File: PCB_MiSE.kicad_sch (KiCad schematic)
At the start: 20 parts, among them IC1 MSP430FR2355TPT, J2 Conn_01x03, SW1 SW_Push, SW2 SW_Push, SW3 SW_Push, U1 LM324, U2 LM324, Y1 Crystal

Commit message: MiSE 24/02
Pendings:
- Check final al sch (comparar con otros grupos).
- Acabar de asignar huellas.
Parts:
- removed R5: R, symbol Device:R
- removed U1, U2: LM324, symbol Amplifier_Operational:LM324
- removed Y1: Crystal, symbol Device:Crystal
- added C5: C, Capacitor_SMD:C_0805_2012Metric_Pad1.18x1.45mm_HandSolder, symbol Device:C
- added J1: WIFI, symbol Connector_Generic:Conn_02x04_Odd_Even
- added J3: Sensor Ultrasonido, symbol Connector_Generic:Conn_01x05
- added J5: Conn_02x07_Counter_Clockwise, symbol Connector_Generic:Conn_02x07_Counter_Clockwise
- added J6: Display, symbol Connector_Generic:Conn_02x04_Odd_Even
- added R10, R11, R8, R9: R, Resistor_SMD:R_0805_2012Metric_Pad1.20x1.40mm_HandSolder, symbol Device:R
- added RV1, RV2: R_Potentiometer_Trim, symbol Device:R_Potentiometer_Trim
- added SW4: SW_Push, Button_Switch_THT:SW_PUSH_6mm, symbol Switch:SW_Push
- added U1: LMV324, Package_SO:SOIC-14_3.9x8.7mm_P1.27mm, symbol Amplifier_Operational:LMV324
- added Y1: Crystal_GND3, Crystal:Crystal_DS26_D2.0mm_L6.0mm_Horizontal_1EP_style1, symbol Device:Crystal_GND3
- C1, C2, C3, C4: footprint (none) -> Capacitor_SMD:C_0805_2012Metric_Pad1.18x1.45mm_HandSolder
- IC1: footprint QFP50P900X900X160-48N -> (none)
- R1, R2, R3, R4, R6, R7: footprint (none) -> Resistor_SMD:R_0805_2012Metric_Pad1.20x1.40mm_HandSolder
- S1: footprint THB001P -> (none)
- SW1, SW2, SW3: footprint (none) -> Button_Switch_THT:SW_PUSH_6mm
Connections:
- net GND: now also C5.2, J1.7 (Pin_7), J3.5 (Pin_5), J5.7 (Pin_7), J5.8 (Pin_8), J6.2 (Pin_2), RV1.2, RV2.2, SW4.1, U1.11 (V-), Y1.3
- net VCC: now also C5.1, J1.2 (Pin_2), J3.1 (Pin_1), J5.1 (Pin_1), J5.14 (Pin_14), J6.1 (Pin_1), R10.1, R11.1, R8.1, R9.1, U1.4 (V+)
- net at S1.12 (2'): now also U1.12 (+), U1.9 (-)
- net at S1.2: now also U1.2 (-), U1.5 (+)
- net at IC1.47 (P3.0/MCLK), S1.C1 (NO_1): now also J5.5 (Pin_5)
- net at C4.1: now also Y1.2
- net at C3.1, IC1.8 (P2.7/TB0CLK/XIN): now also Y1.1
- net at IC1.10 (P2.5/COMP1.0): now also U1.1
- net at R1.2, R2.1: now also U1.10 (+), U1.3 (+)
- net at IC1.13 (P4.6/UCB1SIMO/UCB1SDA): now also U1.8
- net at R2.2, R3.1: now also U1.13 (-), U1.6 (-)
- net at IC1.14 (P4.5/UCB1CLK): now also U1.14
- net at IC1.11 (P2.4/COMP1.1): now also U1.7
- net at IC1.1 (P1.2/UCB0SIMO/UCB0SDA/TB0TRG/OA0-/A2/VEREF-): now also J5.6 (Pin_6), J6.3 (Pin_3)
- net at IC1.2 (P1.1/UCB0CLK/ACLK/OA0O/COMP0.1/A1): now also R8.2, RV2.1
- net at IC1.20 (P6.2/TB3.3): now also J5.13 (Pin_13)
- net at IC1.21 (P6.1/TB3.2): now also J5.12 (Pin_12)
- net at IC1.22 (P6.0/TB3.1): now also J3.2 (Pin_2)
- net at IC1.23 (P4.3/UCA1TXD/UCA1SIMO/~{UCA1TXD}): now also J3.3 (Pin_3)
- net at IC1.31 (P1.7/UCA0TXD/UCA0SIMO/TB0.2/TDO/OA1+/A7/VREF+): now also J1.8 (Pin_8)
- net at IC1.32 (P1.6/UCA0RXD/UCA0SOMI/TB0.1/TDI/TCLK/OA1-/A6): now also J1.1 (Pin_1)
- net at IC1.34 (P1.4/UCA0STE/TCK/A4): now also R11.2, RV1.1
- net at IC1.48 (P1.3/UCB0SOMI/UCB0SCL/OA0+/A3): now also J6.4 (Pin_4)
- new net: J6.5 (Pin_5), R9.2, SW4.2
- new net: J1.6 (Pin_6), R10.2
- no-connect marks 6 -> 46
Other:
- moved on the sheet: C1, C2, C3, C4, IC1, J2, R1, R2, R3, R4, R6, R7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

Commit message: MiSE 24/02
Pendings:
- revisar sch
- actualizar todas las huellas
- poner todos los footprint dentro del proyecto
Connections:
- net GND: now also SW1.1
- net at IC1.5 (~{RST}/NMI/SBWTDIO), J2.2 (Pin_2): now also C1.1, R4.2, SW1.2; no longer SW1.1
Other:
- note removed: "footprint reset: SW_PUSH_6mm"
- moved on the sheet: SW1

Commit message: Add files via upload
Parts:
- removed C5: C, Capacitor_SMD:C_0805_2012Metric_Pad1.18x1.45mm_HandSolder, symbol Device:C
- removed J3: Sensor Ultrasonido, symbol Connector_Generic:Conn_01x05
- removed J5: Conn_02x07_Counter_Clockwise, symbol Connector_Generic:Conn_02x07_Counter_Clockwise
- removed R11, R8: R, Resistor_SMD:R_0805_2012Metric_Pad1.20x1.40mm_HandSolder, symbol Device:R
- added D1: LED, LED_SMD:LED_0805_2012Metric_Pad1.15x1.40mm_HandSolder, symbol Device:LED
- added J4: Clk read conn, Connector_PinHeader_2.54mm:PinHeader_1x02_P2.54mm_Vertical, symbol Connector_Generic:Conn_01x02
- added J7: I2C read, Connector_PinHeader_2.54mm:PinHeader_1x02_P2.54mm_Vertical_SMD_Pin1Left, symbol Connector_Generic:Conn_01x02
- added J8: Conn_02x07_Odd_Even, MSP430:conn_DFrobot, symbol Connector_Generic:Conn_02x07_Odd_Even
- added R12, R13, R14, R5: R, Resistor_SMD:R_0805_2012Metric_Pad1.20x1.40mm_HandSolder, symbol Device:R
- added R15, R8: LDR03, OptoDevice:R_LDR_10x8.5mm_P7.6mm_Vertical, symbol Sensor_Optical:LDR03
- IC1: footprint (none) -> MSP430:QFP50P900X900X160-48N
- J2: footprint (none) -> Connector_PinHeader_2.54mm:PinHeader_1x03_P2.54mm_Vertical
- J6: footprint (none) -> MSP430:LCD_2x16_I2C(Midas)
- RV1, RV2: footprint (none) -> MSP430:Trimmer_MiSE
- S1: footprint (none) -> MSP430:THB001P
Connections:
- net GND: now also S1.C1 (NO_1), J8.13 (Pin_13), J8.14 (Pin_14), R14.2
- net VCC: now also J8.1 (Pin_1), J8.2 (Pin_2), R12.1, R13.1, R15.1, R5.1, R8.1
- net at S1.2, U1.2 (-), U1.5 (+): now also U1.3 (+)
- net at IC1.46 (P3.1/OA2O), S1.B1 (COM_2): now also R5.2
- net at IC1.47 (P3.0/MCLK): no longer S1.C1 (NO_1)
- net TDO/TDI: now reaches C1.1, IC1.5 (~{RST}/NMI/SBWTDIO), R4.2, SW1.2
- net TDO/TDI: now also J2.3 (Pin_3); no longer J2.2 (Pin_2)
- net SDA: now reaches IC1.1 (P1.2/UCB0SIMO/UCB0SDA/TB0TRG/OA0-/A2/VEREF-), J6.3 (Pin_3)
- net SDA: now also J7.1 (Pin_1), J8.11 (Pin_11), R12.2
- net SCL: now reaches IC1.48 (P1.3/UCB0SOMI/UCB0SCL/OA0+/A3), J6.4 (Pin_4)
- net SCL: now also J7.2 (Pin_2), J8.9 (Pin_9), R13.2
- net at C4.1, Y1.2: now also IC1.9 (P2.6/MCLK/XOUT)
- net GPIOl: now reaches U1.7
- net GPIOl: now also IC1.10 (P2.5/COMP1.0); no longer IC1.11 (P2.4/COMP1.1)
- net TCK: now reaches IC1.4 (TEST/SBWTCK)
- net TCK: now also J2.2 (Pin_2); no longer J2.3 (Pin_3)
- net at IC1.34 (P1.4/UCA0STE/TCK/A4), RV1.1: now also R8.2
- net at RV2.1: now also IC1.45 (P3.2/OA2-), R15.2; no longer IC1.2 (P1.1/UCB0CLK/ACLK/OA0O/COMP0.1/A1)
- net at R1.2, R2.1, U1.10 (+): no longer U1.3 (+)
- net P1: now reaches IC1.21 (P6.1/TB3.2)
- net P1: now also J8.6 (Pin_6)
- net P0: now reaches IC1.20 (P6.2/TB3.3)
- net P0: now also J8.4 (Pin_4)
- net CH_EN: now reaches J1.6 (Pin_6), R10.2
- net GPIOr': now reaches IC1.13 (P4.6/UCB1SIMO/UCB1SDA), U1.8
- net GPIOr: now reaches U1.1
- net GPIOr: now also IC1.11 (P2.4/COMP1.1); no longer IC1.10 (P2.5/COMP1.0)
- net U0RXD: now reaches J1.1 (Pin_1)
- net U0RXD: now also IC1.31 (P1.7/UCA0TXD/UCA0SIMO/TB0.2/TDO/OA1+/A7/VREF+); no longer IC1.32 (P1.6/UCA0RXD/UCA0SOMI/TB0.1/TDI/TCLK/OA1-/A6)
- net U0TXD: now reaches J1.8 (Pin_8)
- net U0TXD: now also IC1.32 (P1.6/UCA0RXD/UCA0SOMI/TB0.1/TDI/TCLK/OA1-/A6); no longer IC1.31 (P1.7/UCA0TXD/UCA0SIMO/TB0.2/TDO/OA1+/A7/VREF+)
- net GPIOl': now reaches IC1.14 (P4.5/UCB1CLK), U1.14
- net P8: now reaches IC1.15 (P4.4/UCB1STE)
- net P8: now also J8.10 (Pin_10)
- net P2: now reaches IC1.17 (P6.5/TB3.6)
- net P2: now also J8.8 (Pin_8)
- net at IC1.19 (P6.3/TB3.4): now also D1.2 (A)
- net at IC1.25 (P4.1/UCA1CLK): now also J8.12 (Pin_12)
- net at IC1.3 (P1.0/UCB0STE/SMCLK/COMP0.0/A0/VEREF+): now also J4.1 (Pin_1)
- new net: IC1.2 (P1.1/UCB0CLK/ACLK/OA0O/COMP0.1/A1), J4.2 (Pin_2)
- new net: D1.1 (K), R14.1
- no-connect marks 46 -> 38
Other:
- note added: "Buttons"
- note added: "Conn-Robot"
- note added: "Crystal"
- note added: "Display"
- note added: "Joystick"
- note added: "LDR1"
- note added: "LDR2"
- note added: "RST"
- note added: "SBW"
- note added: "Test-LED"
- note added: "Wi-FI"
- moved on the sheet: C1, C2, C3, C4, IC1, J1, J2, J6, R1, R10, R2, R3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

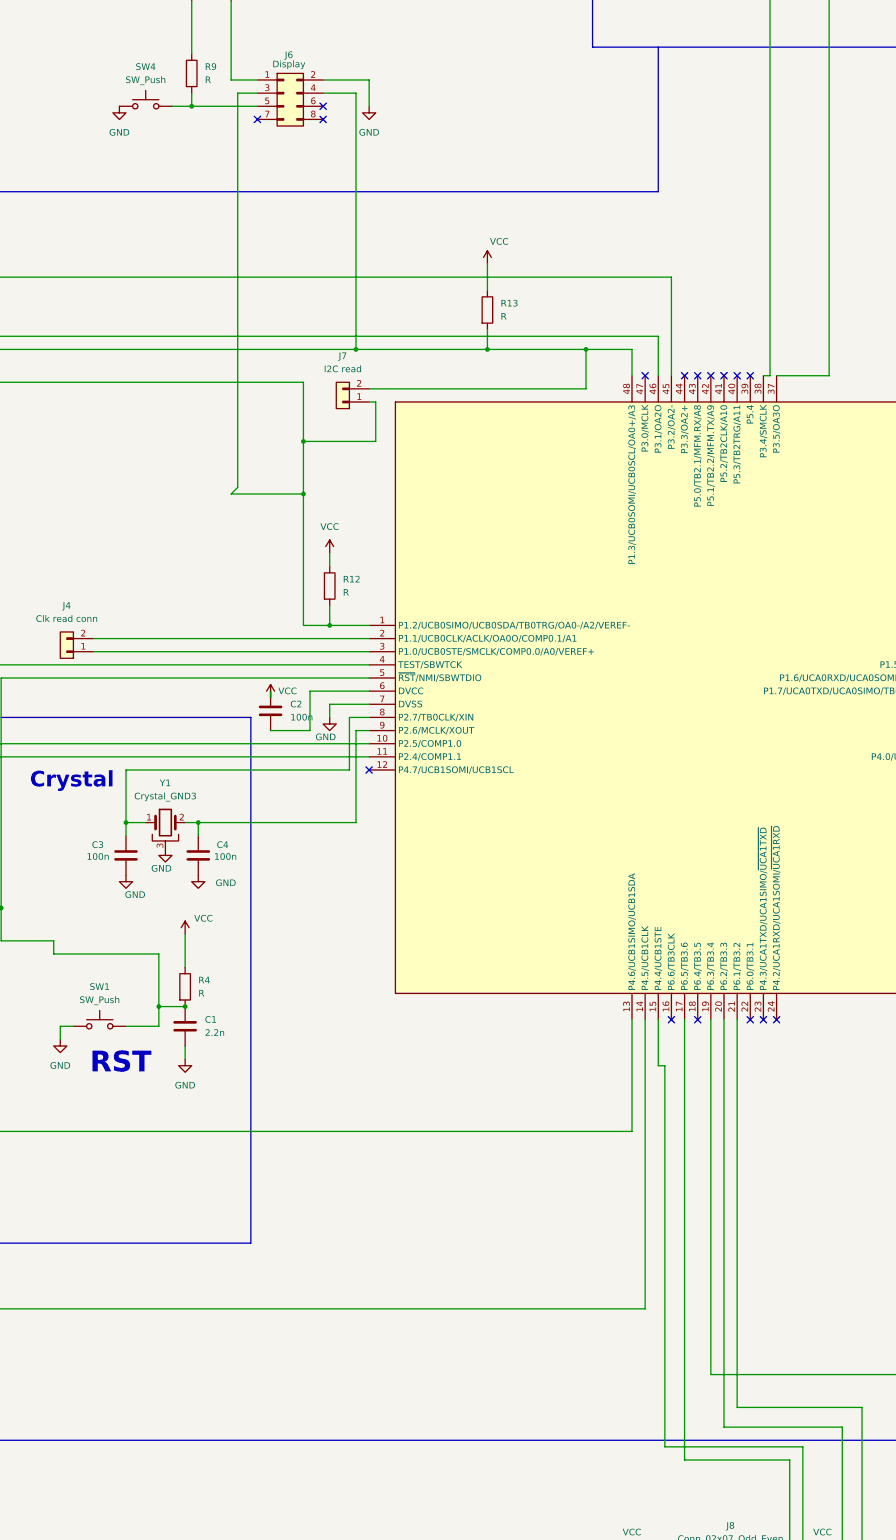
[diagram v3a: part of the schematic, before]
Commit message: Corrijo errores de diseño, DRC bien
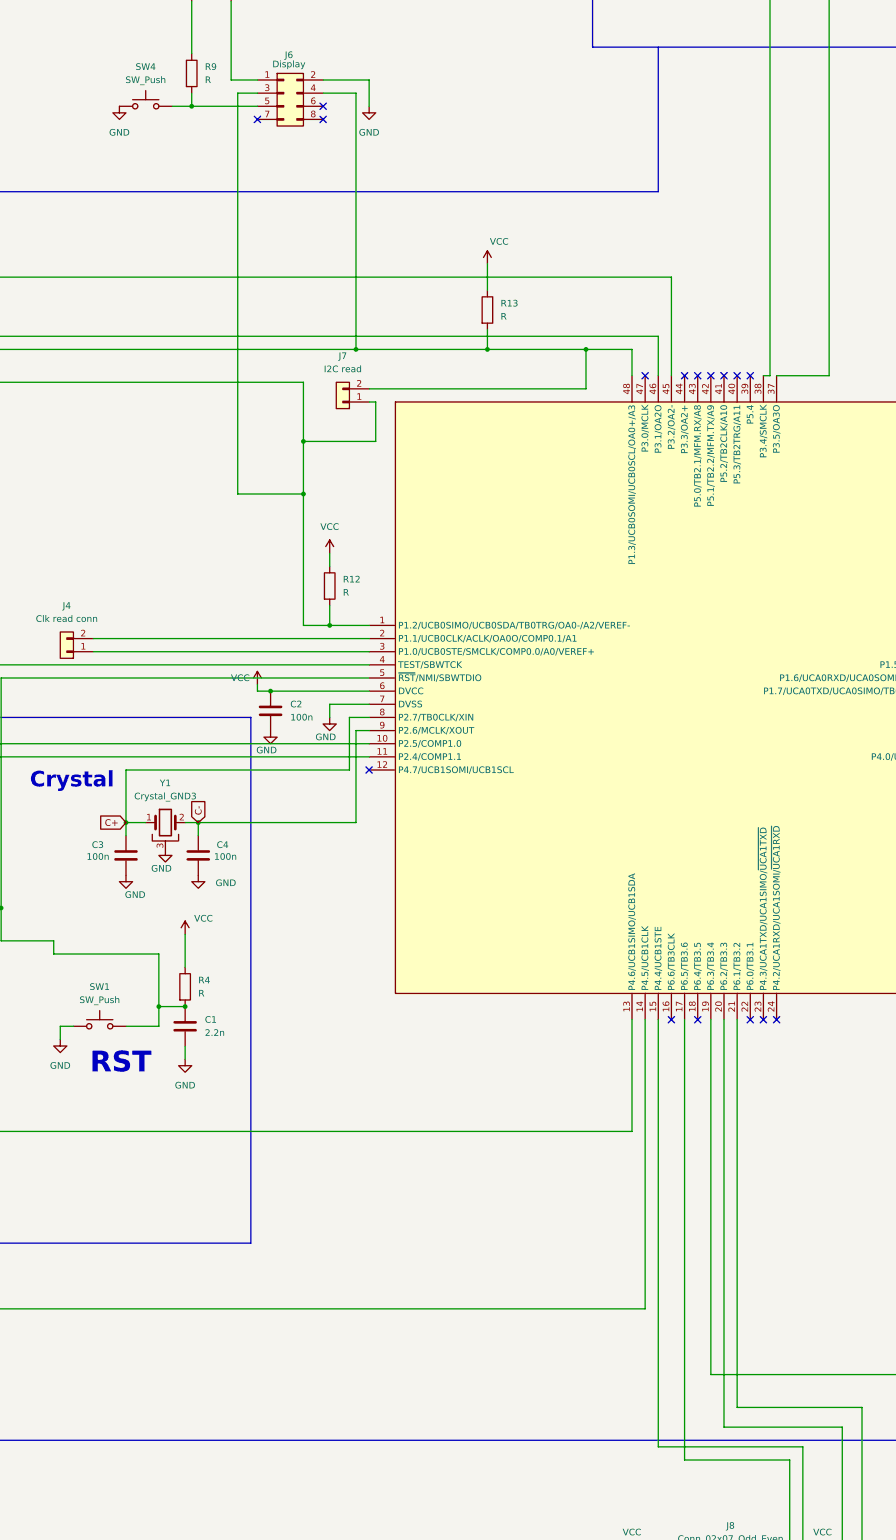
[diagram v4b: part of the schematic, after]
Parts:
- IC1: footprint MSP430:QFP50P900X900X160-48N -> Proyecto:QFP50P900X900X160-48N
- J1: footprint (none) -> Connector_PinHeader_2.54mm:PinHeader_2x04_P2.54mm_Vertical
- J6: footprint MSP430:LCD_2x16_I2C(Midas) -> Proyecto:LCD_2x16_I2C(Midas)
- J8: footprint MSP430:conn_DFrobot -> Proyecto:conn_DFrobot
- R15, R8: footprint OptoDevice:R_LDR_10x8.5mm_P7.6mm_Vertical -> Connector_PinHeader_2.54mm:PinHeader_1x02_P2.54mm_Horizontal
- RV1, RV2: footprint MSP430:Trimmer_MiSE -> Proyecto:Trimmer_MiSE
- S1: footprint MSP430:THB001P -> Proyecto:THB001P
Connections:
- net GND: now also C2.2
- net VCC: now also IC1.6 (DVCC)
- net C-: now reaches C4.1, IC1.9 (P2.6/MCLK/XOUT), Y1.2
- net C+: now reaches C3.1, IC1.8 (P2.7/TB0CLK/XIN), Y1.1
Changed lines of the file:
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@@
 	)
 	(junction
+		(at 227.33 205.74)
+		(diameter 0)
+		(color 0 0 0 0)
+	)
+	(junction
 		(at 269.24 139.7)
 		(diameter 0)
@@
 	(wire
 		(pts
-			(xy 302.26 278.13) (xy 303.53 278.13)
-		)
-		(stroke
-			(width 0)
-			(type default)
-		)
-	)
-	(wire
-		(pts
 			(xy 322.58 381) (xy 327.66 381)
 		)
@@
 	(wire
 		(pts
+			(xy 220.98 167.64) (xy 233.68 167.64)
+		)
+		(stroke
+			(width 0)
+			(type default)
+		)
+	)
+	(wire
+		(pts
 			(xy 101.6 276.86) (xy 101.6 275.59)
 		)
@@
 	(wire
 		(pts
+			(xy 224.79 205.74) (xy 227.33 205.74)
+		)
+		(stroke
+			(width 0)
+			(type default)
+		)
+	)
+	(wire
+		(pts
 			(xy 337.82 375.92) (xy 337.82 373.38)
 		)
@@
 	(wire
 		(pts
-			(xy 234.95 205.74) (xy 246.38 205.74)
+			(xy 227.33 205.74) (xy 246.38 205.74)
 		)
 		(stroke
@@
 	(wire
 		(pts
-			(xy 227.33 213.36) (xy 234.95 213.36)
-		)
-		(stroke
-			(width 0)
-			(type default)
-		)
-	)
-	(wire
-		(pts
 			(xy 36.83 212.09) (xy 43.18 212.09)
 		)
@@
 	(wire
 		(pts
-			(xy 303.53 351.79) (xy 330.2 351.79)
+			(xy 302.26 351.79) (xy 330.2 351.79)
 		)
 		(stroke
@@
 	(wire
 		(pts
-			(xy 220.98 90.17) (xy 220.98 166.37)
+			(xy 220.98 90.17) (xy 220.98 167.64)
 		)
 		(stroke
@@
 	(wire
 		(pts
-			(xy 302.26 269.24) (xy 302.26 278.13)
+			(xy 302.26 269.24) (xy 302.26 351.79)
 		)
 		(stroke
@@
 	(wire
 		(pts
-			(xy 303.53 278.13) (xy 303.53 351.79)
-		)
-		(stroke
-			(width 0)
-			(type default)
-		)
-	)
-	(wire
-		(pts
 			(xy 224.79 87.63) (xy 219.71 87.63)
 		)
@@
 	(wire
 		(pts
-			(xy 227.33 207.01) (xy 227.33 205.74)
+			(xy 224.79 204.47) (xy 224.79 205.74)
 		)
 		(stroke
@@
 	(wire
 		(pts
-			(xy 219.71 167.64) (xy 233.68 167.64)
-		)
-		(stroke
-			(width 0)
-			(type default)
-		)
-	)
-	(wire
-		(pts
 			(xy 238.76 193.04) (xy 246.38 193.04)
 		)
@@
 	(wire
 		(pts
-			(xy 234.95 205.74) (xy 234.95 213.36)
-		)
-		(stroke
-			(width 0)
-			(type default)
-		)
-	)
-	(wire
-		(pts
 			(xy 481.33 99.06) (xy 499.11 99.06)
 		)
@@
 	(wire
 		(pts
-			(xy 220.98 166.37) (xy 219.71 167.64)
-		)
-		(stroke
-			(width 0)
-			(type default)
-		)
-	)
-	(wire
-		(pts
 			(xy 50.8 125.73) (xy 50.8 128.27)
 		)
@@
 		)
 	)
+	(global_label "C+"
+		(shape input)
+		(at 199.39 231.14 180)
+		(fields_autoplaced yes)
+		(effects
+			(font
+				(size 1.27 1.27)
+			)
+			(justify right)
+		)
+		(property "Intersheetrefs" "${INTERSHEET_REFS}"
+			(at 193.5624 231.14 0)
+			(effects
+				(font
+					(size 1.27 1.27)
+				)
+				(justify right)
+				(hide yes)
+			)
+		)
+	)
+	(global_label "C-"
+		(shape input)
+		(at 213.36 231.14 90)
+		(fields_autoplaced yes)
+		(effects
+			(font
+				(size 1.27 1.27)
+			)
+			(justify left)
+		)
+		(property "Intersheetrefs" "${INTERSHEET_REFS}"
+			(at 213.36 225.3124 90)
+			(effects
+				(font
+					(size 1.27 1.27)
+				)
+				(justify left)
+				(hide yes)
+			)
+		)
+	)
 	(global_label "GPIOl'"
 		(shape input)
@@
 			)
 		)
-		(property "Footprint" "MSP430:THB001P"
+		(property "Footprint" "Proyecto:THB001P"
 			(at 69.85 307.01 0)
 			(effects
@@
 			)
 		)
-		(property "Footprint" "MSP430:LCD_2x16_I2C(Midas)"
+		(property "Footprint" "Proyecto:LCD_2x16_I2C(Midas)"
 			(at 229.87 90.17 0)
 			(effects
@@
 	(symbol
 		(lib_id "power:GND")
+		(at 227.33 213.36 0)
+		(unit 1)
+		(exclude_from_sim no)
+		(in_bom yes)
+		(on_board yes)
+		(dnp no)
+		(property "Reference" "#PWR024"
+			(at 227.33 219.71 0)
+			(effects
+				(font
+					(size 1.27 1.27)
+				)
+				(hide yes)
+			)
+		)
+		(property "Value" "GND"
+			(at 226.568 217.17 0)
+			(effects
+				(font
+					(size 1.27 1.27)
+				)
+			)
+		)
+		(property "Footprint" ""
+			(at 227.33 213.36 0)
+			(effects
+				(font
+					(size 1.27 1.27)
+				)
+				(hide yes)
+			)
+		)
+		(property "Datasheet" ""
+			(at 227.33 213.36 0)
+			(effects
+				(font
+					(size 1.27 1.27)
+				)
+				(hide yes)
+			)
+		)
+		(property "Description" "Power symbol creates a global label with name \"GND\" , ground"
+			(at 227.33 213.36 0)
+			(effects
+				(font
+					(size 1.27 1.27)
+				)
+				(hide yes)
+			)
+		)
+		(pin "1"
+		)
+		(instances
+			(project "PCB_MiSE"
+				(path "/d767662d-a2fb-4431-89c7-c67b7c23601b"
+					(reference "#PWR024")
+					(unit 1)
+				)
+			)
+		)
+	)
+	(symbol
+		(lib_id "power:GND")
 		(at 186.69 273.05 0)
 		(unit 1)
@@
 	(symbol
 		(lib_id "power:VCC")
-		(at 227.33 207.01 0)
+		(at 224.79 204.47 0)
+		(mirror y)
 		(unit 1)
 		(exclude_from_sim no)
@@
 		(dnp no)
 		(property "Reference" "#PWR010"
-			(at 227.33 210.82 0)
+			(at 224.79 208.28 0)
 			(effects
 				(font
@@
 		)
 		(property "Value" "VCC"
-			(at 230.632 205.74 0)
+			(at 221.488 203.2 0)
 			(effects
 				(font
@@
 		)
 		(property "Footprint" ""
-			(at 227.33 207.01 0)
+			(at 224.79 204.47 0)
 			(effects
 				(font
@@
 		)
 		(property "Datasheet" ""
-			(at 227.33 207.01 0)
+			(at 224.79 204.47 0)
 			(effects
 				(font
@@
 		)
 		(property "Description" "Power symbol creates a global label with name \"VCC\""
-			(at 227.33 207.01 0)
+			(at 224.79 204.47 0)
 			(effects
 				(font
@@
 			)
 		)
-		(property "Footprint" "MSP430:Trimmer_MiSE"
+		(property "Footprint" "Proyecto:Trimmer_MiSE"
 			(at 499.11 105.41 0)
 			(effects
@@
 			)
 		)
-		(property "Footprint" "MSP430:Trimmer_MiSE"
+		(property "Footprint" "Proyecto:Trimmer_MiSE"
 			(at 50.8 132.08 0)
 			(effects
@@
 			)
 		)
-		(property "Footprint" "OptoDevice:R_LDR_10x8.5mm_P7.6mm_Vertical"
+		(property "Footprint" "Connector_PinHeader_2.54mm:PinHeader_1x02_P2.54mm_Horizontal"
 			(at 55.245 119.38 90)
 			(effects
@@
 			)
 		)
-		(property "Footprint" ""
+		(property "Footprint" "Connector_PinHeader_2.54mm:PinHeader_2x04_P2.54mm_Vertical"
 			(at 548.64 222.25 0)
 			(effects
@@
 			)
 		)
-		(property "Footprint" "MSP430:conn_DFrobot"
+		(property "Footprint" "Proyecto:conn_DFrobot"
 			(at 314.96 381 0)
 			(effects
@@
 			)
 		)
-		(property "Footprint" "OptoDevice:R_LDR_10x8.5mm_P7.6mm_Vertical"
+		(property "Footprint" "Connector_PinHeader_2.54mm:PinHeader_1x02_P2.54mm_Horizontal"
 			(at 503.555 93.98 90)
 			(effects
@@
 			)
 		)
-		(property "Footprint" "MSP430:QFP50P900X900X160-48N"
+		(property "Footprint" "Proyecto:QFP50P900X900X160-48N"
 			(at 372.11 247.32 0)
 			(effects

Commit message: muevo los conectores segun dijo Pep
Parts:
- removed J7: I2C read, Connector_PinHeader_2.54mm:PinHeader_1x02_P2.54mm_Vertical_SMD_Pin1Left, symbol Connector_Generic:Conn_01x02
- added J10, J11, J3, J5, J7, J9: Conn_01x01, Connector_PinHeader_2.54mm:PinHeader_1x01_P2.54mm_Vertical, symbol Connector_Generic:Conn_01x01
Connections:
- net GND: now also J7.1 (Pin_1), J9.1 (Pin_1)
- net SCL: now also J3.1 (Pin_1)
- net SDA: now also J5.1 (Pin_1)
- net U0RXD: now also J10.1 (Pin_1)
- net U0TXD: now also J11.1 (Pin_1)
